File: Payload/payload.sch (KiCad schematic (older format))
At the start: 33 parts

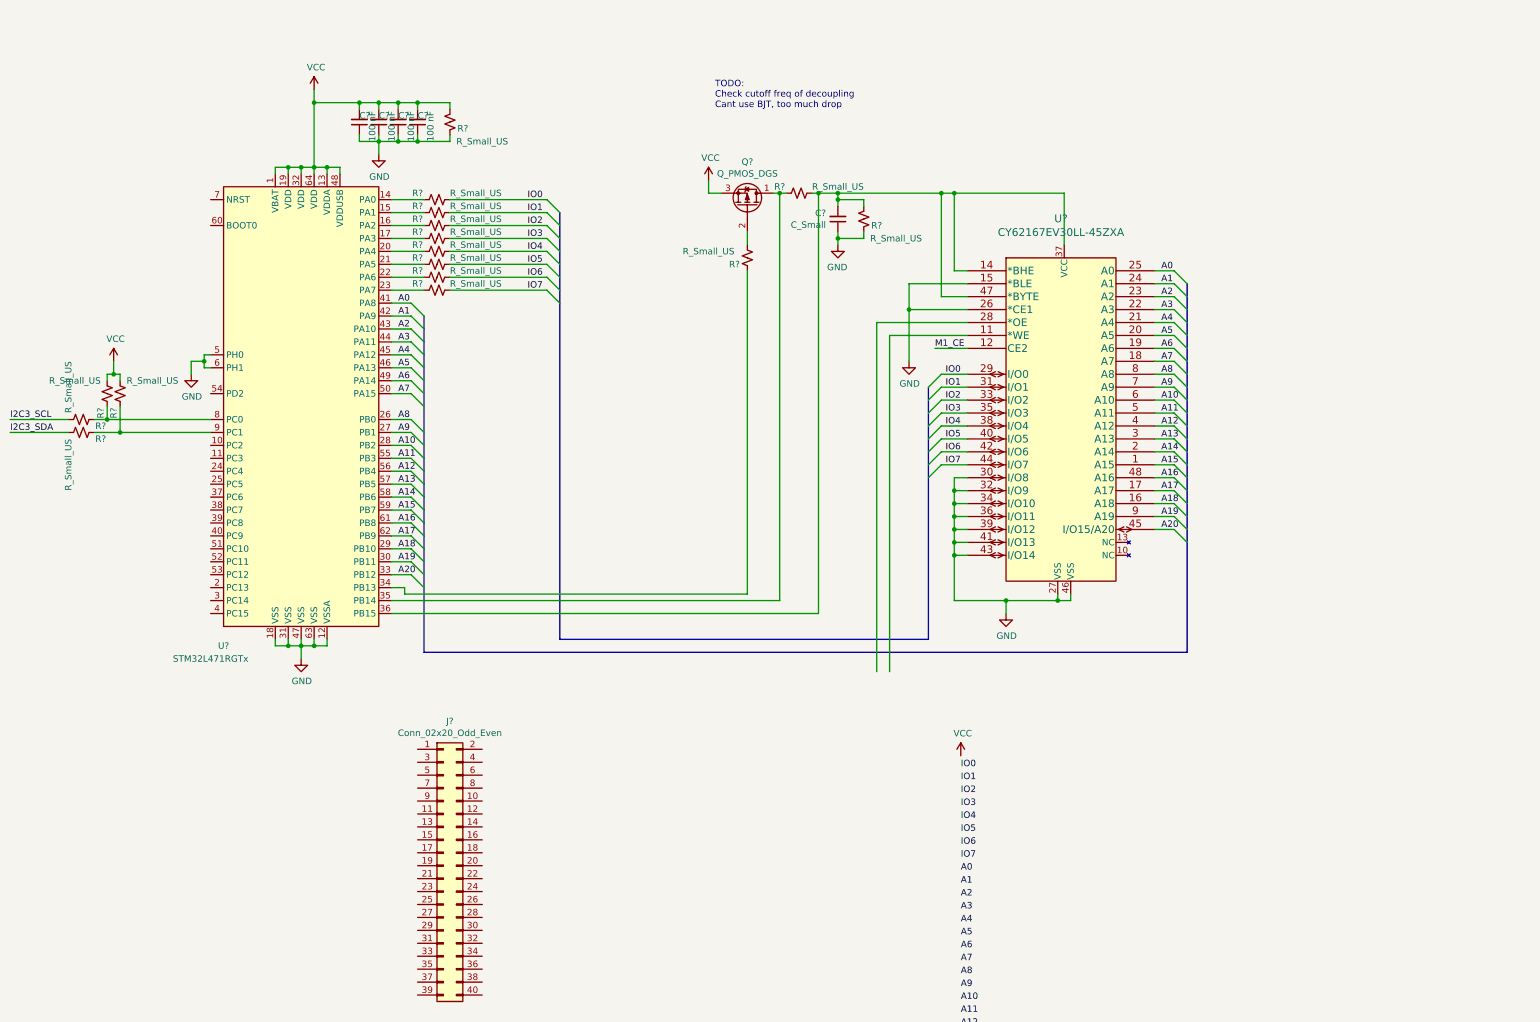
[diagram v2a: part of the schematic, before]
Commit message: Hook up chip controls and some power stuff
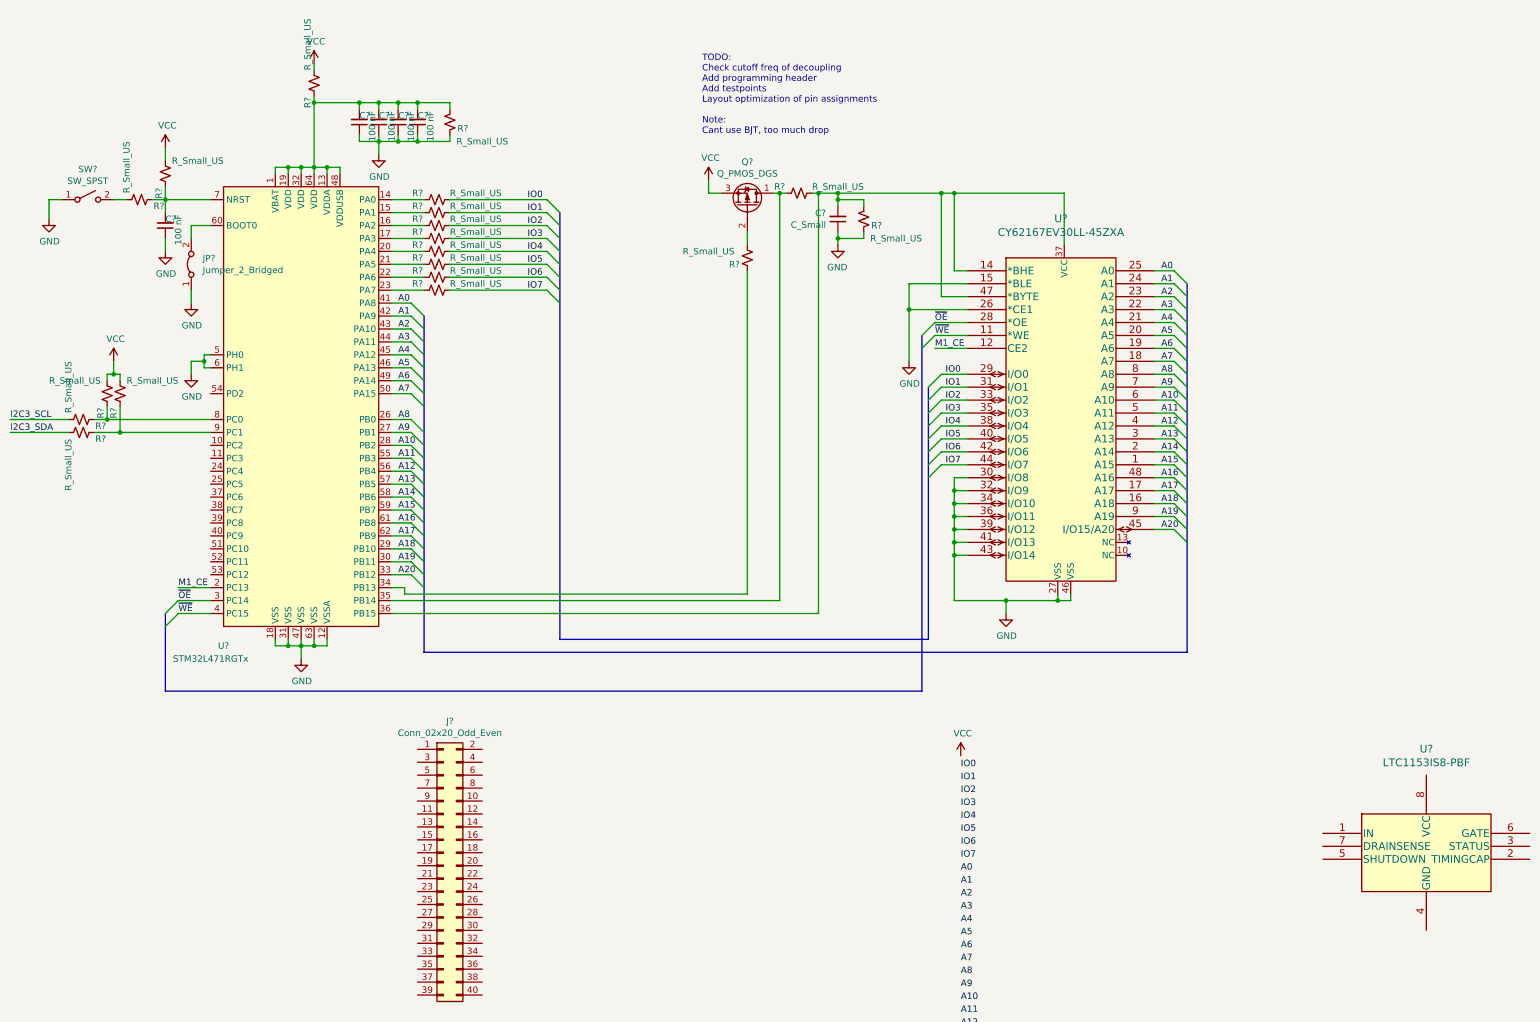
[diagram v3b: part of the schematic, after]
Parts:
- added C?: 100 nF, symbol Device:C_Small
- added JP?: Jumper_2_Bridged, symbol Jumper:Jumper_2_Bridged
- added R? (x3): R_Small_US, symbol Device:R_Small_US
- added SW?: SW_SPST, symbol Switch:SW_SPST
- added U?: LTC1153IS8-PBF, SOIC-8_S_LIT, symbol Payload2:LTC1153IS8-PBF
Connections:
- net GND: now also C?.1, JP?.1 (A), SW?.1 (A)
- net M1_CE: now also U?.2 (PC13)
- net VCC: now also R?.1, R?.2; no longer C?.2, C?.2, C?.2, C?.2, R?.1, U?.1 (VBAT), U?.13 (VDDA), U?.19 (VDD), U?.32 (VDD), U?.48 (VDDUSB), U?.64 (VDD)
- net ~OE: now reaches U?.3 (PC14)
- net ~OE: now also U?.28 (*OE)
- net ~WE: now reaches U?.4 (PC15)
- net ~WE: now also U?.11 (*WE)
- net at U?.60 (BOOT0): now also JP?.2 (B)
- net at U?.7 (NRST): now also C?.2, R?.2, R?.2
- new net: C?.2, C?.2, C?.2, C?.2, R?.1, R?.1, U?.1 (VBAT), U?.13 (VDDA), U?.19 (VDD), U?.32 (VDD), U?.48 (VDDUSB), U?.64 (VDD)
- new net: R?.1, SW?.2 (B)
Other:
- note added: "TODO:\nCheck cutoff freq of decoupling\nAdd programming header\nAdd testpoints\nLayout optimization of pin assignments\n\nNote:\nCant use BJT, too much drop"
- note removed: "TODO:\nCheck cutoff freq of decoupling\nCant use BJT, too much drop"
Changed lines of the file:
@@
 encoding utf-8
 Sheet 1 1
-Title ""
+Title "Payload Two"
 Date ""
 Rev ""
 Comp ""
-Comment1 ""
+Comment1 "Daniel Stutman - 2021"
 Comment2 ""
 Comment3 ""
@@
 Wire Wire Line
 	6350 2250 6350 2350
-Text Notes 6100 1300 0    50   ~ 0
-TODO:\nCheck cutoff freq of decoupling\nCant use BJT, too much drop
+Text Notes 6000 1500 0    50   ~ 0
+TODO:\nCheck cutoff freq of decoupling\nAdd programming header\nAdd testpoints\nLayout optimization of pin assignments\n\nNote:\nCant use BJT, too much drop
 Wire Wire Line
 	8750 5050 8750 5100
@@
 Wire Wire Line
 	3000 1250 3000 1750
-Wire Wire Line
-	3000 1250 3000 1150
-Connection ~ 3000 1250
 $Comp
 L power:VCC #PWR?
 U 1 1 60725407
-P 3000 1150
-F 0 "#PWR?" H 3000 1000 50  0001 C CNN
-F 1 "VCC" H 3015 1323 50  0000 C CNN
-F 2 "" H 3000 1150 50  0001 C CNN
-F 3 "" H 3000 1150 50  0001 C CNN
-	1    3000 1150
+P 3000 950
+F 0 "#PWR?" H 3000 800 50  0001 C CNN
+F 1 "VCC" H 3015 1123 50  0000 C CNN
+F 2 "" H 3000 950 50  0001 C CNN
+F 3 "" H 3000 950 50  0001 C CNN
+	1    3000 950
 	1    0    0    -1
 $EndComp
@@
 Wire Bus Line
 	7750 5400 4900 5400
-Wire Wire Line
-	8050 3050 7450 3050
-Wire Wire Line
-	8050 2950 7350 2950
 Text Label 7800 3150 0    50   ~ 0
 M1_CE
@@
 $EndComp
 Wire Wire Line
-	7350 2950 7350 5650
-Wire Wire Line
-	7450 3050 7450 5650
-Wire Wire Line
 	1400 3700 2200 3700
 Wire Wire Line
 	1500 3800 2200 3800
+$Comp
+L Payload2:LTC1153IS8-PBF U?
+U 1 1 6052ADAC
+P 11600 7000
+F 0 "U?" H 11600 7753 60  0000 C CNN
+F 1 "LTC1153IS8-PBF" H 11600 7647 60  0000 C CNN
+F 2 "SOIC-8_S_LIT" H 12500 7240 60  0001 C CNN
+F 3 "" H 10800 7100 60  0000 C CNN
+	1    11600 7000
+	1    0    0    -1
+$EndComp
+$Comp
+L Device:R_Small_US R?
+U 1 1 60546454
+P 1650 2000
+F 0 "R?" V 1600 1850 50  0000 C CNN
+F 1 "R_Small_US" H 1900 2100 50  0000 C CNN
+F 2 "" H 1650 2000 50  0001 C CNN
+F 3 "~" H 1650 2000 50  0001 C CNN
+	1    1650 2000
+	0    -1   -1   0
+$EndComp
+$Comp
+L Device:C_Small C?
+U 1 1 6055F678
+P 1850 2200
+F 0 "C?" H 1850 2150 50  0000 R CNN
+F 1 "100 nF" V 1750 2350 50  0000 R CNN
+F 2 "" H 1850 2200 50  0001 C CNN
+F 3 "~" H 1850 2200 50  0001 C CNN
+	1    1850 2200
+	-1   0    0    1
+$EndComp
+$Comp
+L Device:R_Small_US R?
+U 1 1 605900BB
+P 1850 1800
+F 0 "R?" V 1800 1650 50  0000 C CNN
+F 1 "R_Small_US" H 2100 1900 50  0000 C CNN
+F 2 "" H 1850 1800 50  0001 C CNN
+F 3 "~" H 1850 1800 50  0001 C CNN
+	1    1850 1800
+	1    0    0    -1
+$EndComp
+Wire Wire Line
+	1750 2000 1850 2000
+Wire Wire Line
+	1850 2000 1850 1900
+Wire Wire Line
+	1850 2000 1850 2100
+$Comp
+L power:GND #PWR?
+U 1 1 605C0FA7
+P 1850 2400
+F 0 "#PWR?" H 1850 2150 50  0001 C CNN
+F 1 "GND" H 1855 2227 50  0000 C CNN
+F 2 "" H 1850 2400 50  0001 C CNN
+F 3 "" H 1850 2400 50  0001 C CNN
+	1    1850 2400
+	1    0    0    -1
+$EndComp
+Wire Wire Line
+	1850 2400 1850 2300
+$Comp
+L power:VCC #PWR?
+U 1 1 605CE630
+P 1850 1600
+F 0 "#PWR?" H 1850 1450 50  0001 C CNN
+F 1 "VCC" H 1865 1773 50  0000 C CNN
+F 2 "" H 1850 1600 50  0001 C CNN
+F 3 "" H 1850 1600 50  0001 C CNN
+	1    1850 1600
+	1    0    0    -1
+$EndComp
+Wire Wire Line
+	1850 1600 1850 1700
+$Comp
+L Switch:SW_SPST SW?
+U 1 1 605DC322
+P 1250 2000
+F 0 "SW?" H 1250 2235 50  0000 C CNN
+F 1 "SW_SPST" H 1250 2144 50  0000 C CNN
+F 2 "" H 1250 2000 50  0001 C CNN
+F 3 "~" H 1250 2000 50  0001 C CNN
+	1    1250 2000
+	1    0    0    -1
+$EndComp
+Wire Wire Line
+	1450 2000 1550 2000
+$Comp
+L power:GND #PWR?
+U 1 1 60605C42
+P 950 2150
+F 0 "#PWR?" H 950 1900 50  0001 C CNN
+F 1 "GND" H 955 1977 50  0000 C CNN
+F 2 "" H 950 2150 50  0001 C CNN
+F 3 "" H 950 2150 50  0001 C CNN
+	1    950  2150
+	1    0    0    -1
+$EndComp
+Wire Wire Line
+	950  2000 1050 2000
+Wire Wire Line
+	950  2000 950  2150
+Connection ~ 1850 2000
+Wire Wire Line
+	1850 2000 2200 2000
+$Comp
+L Jumper:Jumper_2_Bridged JP?
+U 1 1 60656522
+P 2050 2500
+F 0 "JP?" V 2096 2412 50  0000 R CNN
+F 1 "Jumper_2_Bridged" V 2005 2412 50  0000 R CNN
+F 2 "" H 2050 2500 50  0001 C CNN
+F 3 "~" H 2050 2500 50  0001 C CNN
+	1    2050 2500
+	0    -1   -1   0
+$EndComp
+Wire Wire Line
+	2050 2200 2050 2300
+$Comp
+L power:GND #PWR?
+U 1 1 60666794
+P 2050 2800
+F 0 "#PWR?" H 2050 2550 50  0001 C CNN
+F 1 "GND" H 2055 2627 50  0000 C CNN
+F 2 "" H 2050 2800 50  0001 C CNN
+F 3 "" H 2050 2800 50  0001 C CNN
+	1    2050 2800
+	1    0    0    -1
+$EndComp
+Wire Wire Line
+	2050 2700 2050 2800
+Wire Wire Line
+	2050 2200 2200 2200
+Wire Wire Line
+	7800 3050 8050 3050
+Entry Wire Line
+	7800 2950 7700 3050
+Wire Wire Line
+	7800 2950 8050 2950
+Text Label 7800 3050 0    50   ~ 0
+~WE
+Text Label 7800 2950 0    50   ~ 0
+~OE
+Entry Wire Line
+	7800 3050 7700 3150
+Wire Wire Line
+	1950 5200 2200 5200
+Entry Wire Line
+	1950 5100 1850 5200
+Wire Wire Line
+	1950 5100 2200 5100
+Text Label 1950 5200 0    50   ~ 0
+~WE
+Text Label 1950 5100 0    50   ~ 0
+~OE
+Entry Wire Line
+	1950 5200 1850 5300
+Wire Bus Line
+	7700 5800 1850 5800
+Text Label 1950 5000 0    50   ~ 0
+M1_CE
+Wire Wire Line
+	1950 5000 2200 5000
+$Comp
+L Device:R_Small_US R?
+U 1 1 607AC261
+P 3000 1100
+F 0 "R?" V 3050 1250 50  0000 C CNN
+F 1 "R_Small_US" V 3050 800 50  0000 C CNN
+F 2 "" H 3000 1100 50  0001 C CNN
+F 3 "~" H 3000 1100 50  0001 C CNN
+	1    3000 1100
+	-1   0    0    1
+$EndComp
+Wire Wire Line
+	3000 1200 3000 1250
+Connection ~ 3000 1250
+Wire Wire Line
+	3000 1000 3000 950
+Wire Bus Line
+	7700 3050 7700 5800
+Wire Bus Line
+	1850 5200 1850 5800
 Wire Bus Line
 	4900 2100 4900 5400

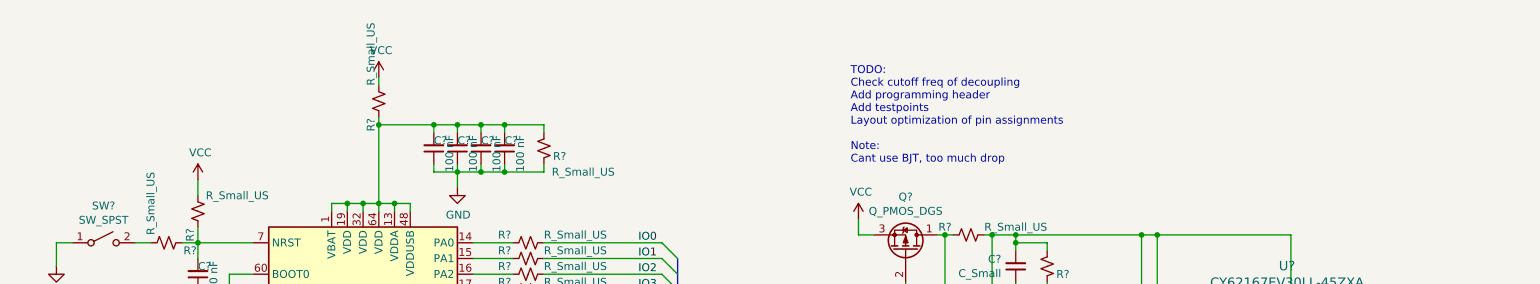
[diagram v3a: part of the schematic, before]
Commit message: Current limiting resistor and implementation notes
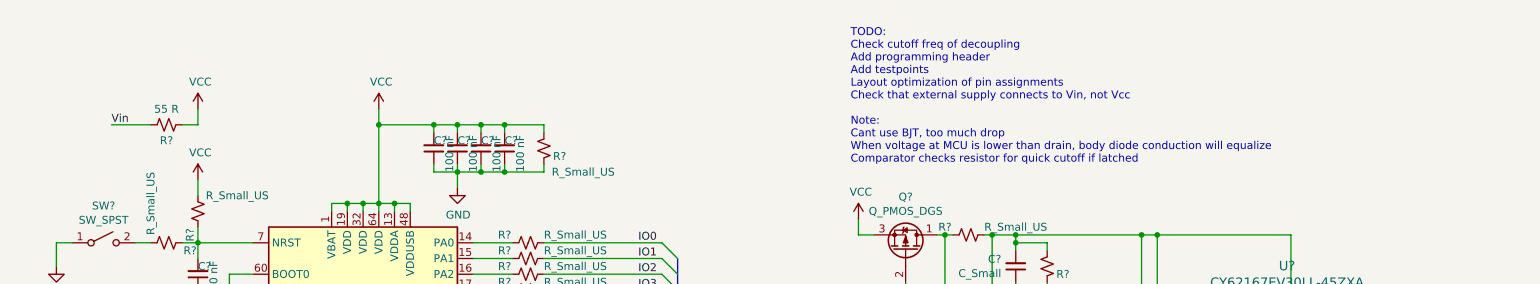
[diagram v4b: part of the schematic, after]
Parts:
- R?: value R_Small_US -> 55 R
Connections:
- net VCC: now also C?.2, C?.2, C?.2, C?.2, R?.1, R?.1, U?.1 (VBAT), U?.13 (VDDA), U?.19 (VDD), U?.32 (VDD), U?.48 (VDDUSB), U?.64 (VDD); no longer R?.2
- new net Vin: R?.2
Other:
- note added: "TODO:\nCheck cutoff freq of decoupling\nAdd programming header\nAdd testpoints\nLayout optimization of pin assignments\nCheck that external supply connects to Vin, not Vcc\n\nNote:\nCant use BJT, too much drop\nWhen voltage at MCU is lower than drain, body diode conduction will equalize\nComparator checks resistor for quick cutoff if latched"
- note removed: "TODO:\nCheck cutoff freq of decoupling\nAdd programming header\nAdd testpoints\nLayout optimization of pin assignments\n\nNote:\nCant use BJT, too much drop"
- moved on the sheet: R?
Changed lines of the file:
@@
 	6350 2250 6350 2350
 Text Notes 6000 1500 0    50   ~ 0
-TODO:\nCheck cutoff freq of decoupling\nAdd programming header\nAdd testpoints\nLayout optimization of pin assignments\n\nNote:\nCant use BJT, too much drop
+TODO:\nCheck cutoff freq of decoupling\nAdd programming header\nAdd testpoints\nLayout optimization of pin assignments\nCheck that external supply connects to Vin, not Vcc\n\nNote:\nCant use BJT, too much drop\nWhen voltage at MCU is lower than drain, body diode conduction will equalize\nComparator checks resistor for quick cutoff if latched
 Wire Wire Line
 	8750 5050 8750 5100
@@
 L power:VCC #PWR?
 U 1 1 60725407
-P 3000 950
-F 0 "#PWR?" H 3000 800 50  0001 C CNN
-F 1 "VCC" H 3015 1123 50  0000 C CNN
-F 2 "" H 3000 950 50  0001 C CNN
-F 3 "" H 3000 950 50  0001 C CNN
-	1    3000 950
+P 3000 1150
+F 0 "#PWR?" H 3000 1000 50  0001 C CNN
+F 1 "VCC" H 3015 1323 50  0000 C CNN
+F 2 "" H 3000 1150 50  0001 C CNN
+F 3 "" H 3000 1150 50  0001 C CNN
+	1    3000 1150
 	1    0    0    -1
 $EndComp
@@
 L Device:R_Small_US R?
 U 1 1 607AC261
-P 3000 1100
-F 0 "R?" V 3050 1250 50  0000 C CNN
-F 1 "R_Small_US" V 3050 800 50  0000 C CNN
-F 2 "" H 3000 1100 50  0001 C CNN
-F 3 "~" H 3000 1100 50  0001 C CNN
-	1    3000 1100
-	-1   0    0    1
-$EndComp
-Wire Wire Line
-	3000 1200 3000 1250
+P 1650 1250
+F 0 "R?" V 1750 1250 50  0000 C CNN
+F 1 "55 R" V 1550 1250 50  0000 C CNN
+F 2 "" H 1650 1250 50  0001 C CNN
+F 3 "~" H 1650 1250 50  0001 C CNN
+	1    1650 1250
+	0    1    1    0
+$EndComp
 Connection ~ 3000 1250
 Wire Wire Line
-	3000 1000 3000 950
+	3000 1150 3000 1250
+Text Label 1300 1250 0    50   ~ 0
+Vin
+Wire Wire Line
+	1550 1250 1300 1250
+$Comp
+L power:VCC #PWR?
+U 1 1 60669A2E
+P 1850 1150
+F 0 "#PWR?" H 1850 1000 50  0001 C CNN
+F 1 "VCC" H 1865 1323 50  0000 C CNN
+F 2 "" H 1850 1150 50  0001 C CNN
+F 3 "" H 1850 1150 50  0001 C CNN
+	1    1850 1150
+	1    0    0    -1
+$EndComp
+Wire Wire Line
+	1750 1250 1850 1250
+Wire Wire Line
+	1850 1250 1850 1150
 Wire Bus Line
 	7700 3050 7700 5800

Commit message: Add additional TODO
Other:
- note added: "TODO:\nCheck cutoff freq of decoupling\nAdd programming header\nAdd testpoints\nLayout optimization of pin assignments\nCheck that external supply connects to Vin, not Vcc\nActually connect sense resistor pins for memory power\nto comparator pins\n\nNote:\nCant use BJT, too much drop\nWhen voltage at MCU is lower than drain, body diode conduction will equalize\nComparator checks resistor for quic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"
- note removed: "TODO:\nCheck cutoff freq of decoupling\nAdd programming header\nAdd testpoints\nLayout optimization of pin assignments\nCheck that external supply connects to Vin, not Vcc\n\nNote:\nCant use BJT, too much drop\nWhen voltage at MCU is lower than drain, body diode conduction will equalize\nComparator checks resistor for quick cutoff if latched"
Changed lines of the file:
@@
 Wire Wire Line
 	6350 2250 6350 2350
-Text Notes 6000 1500 0    50   ~ 0
-TODO:\nCheck cutoff freq of decoupling\nAdd programming header\nAdd testpoints\nLayout optimization of pin assignments\nCheck that external supply connects to Vin, not Vcc\n\nNote:\nCant use BJT, too much drop\nWhen voltage at MCU is lower than drain, body diode conduction will equalize\nComparator checks resistor for quick cutoff if latched
+Text Notes 6000 1550 0    50   ~ 0
+TODO:\nCheck cutoff freq of decoupling\nAdd programming header\nAdd testpoints\nLayout optimization of pin assignments\nCheck that external supply connects to Vin, not Vcc\nActually connect sense resistor pins for memory power\nto comparator pins\n\nNote:\nCant use BJT, too much drop\nWhen voltage at MCU is lower than drain, body diode conduction will equalize\nComparator checks resistor for quick cutoff if latched
 Wire Wire Line
 	8750 5050 8750 5100
